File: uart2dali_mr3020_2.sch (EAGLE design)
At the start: 79 parts, among them IC2 LM393D, IC3 SFH6156, IC4 SFH6156, J1 AVR_SPI_PRG_6NS, Q1 SST201, Q2 BSP170P, Q3 BC817-25SMD, X1 SM04B-SRSS-TB

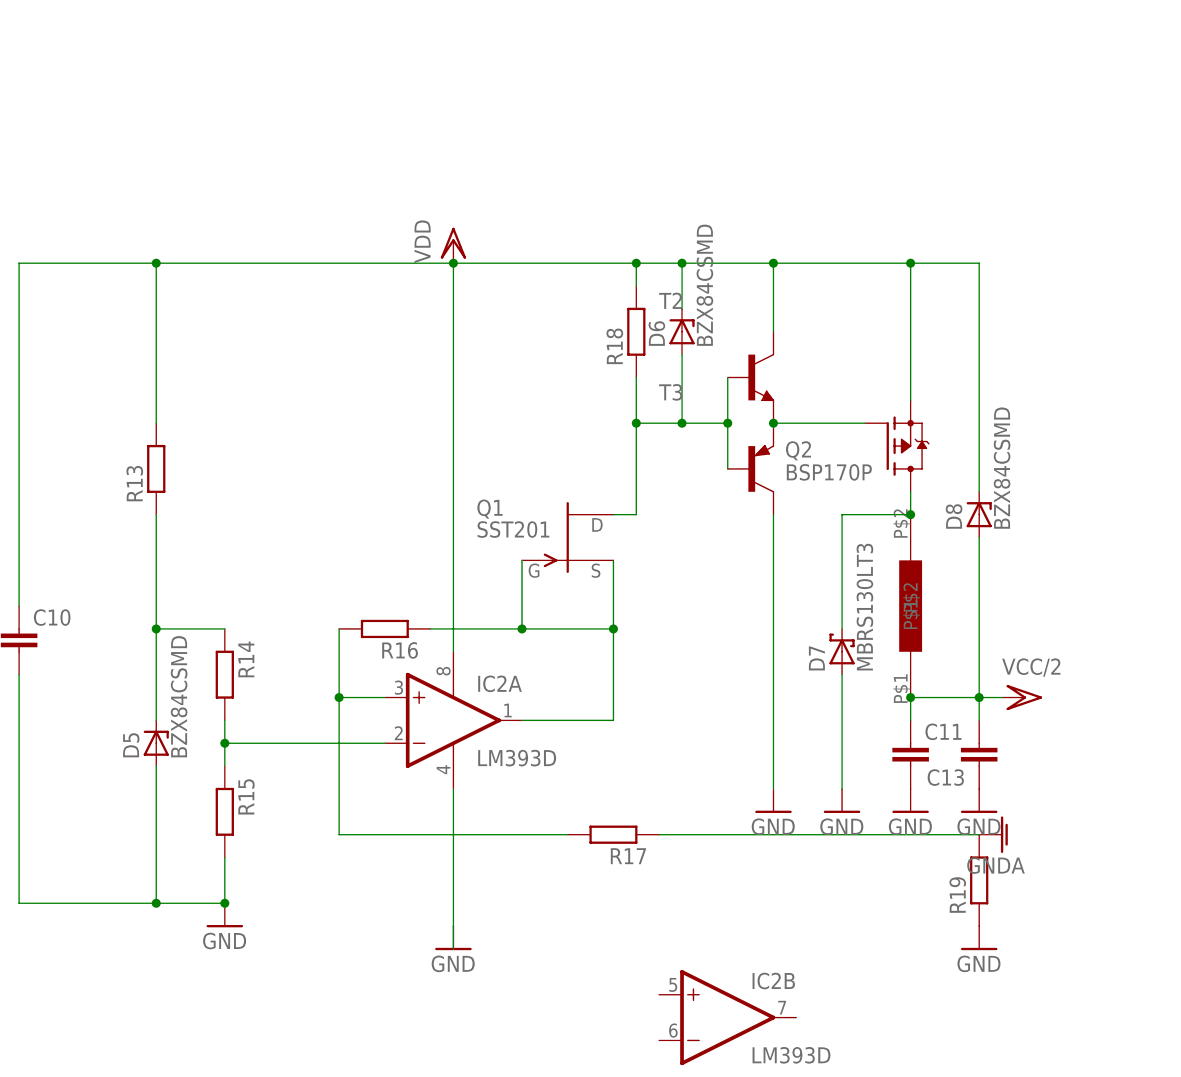
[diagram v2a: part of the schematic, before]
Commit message: - added values parts of constant current circuit - dali master can query from slaves
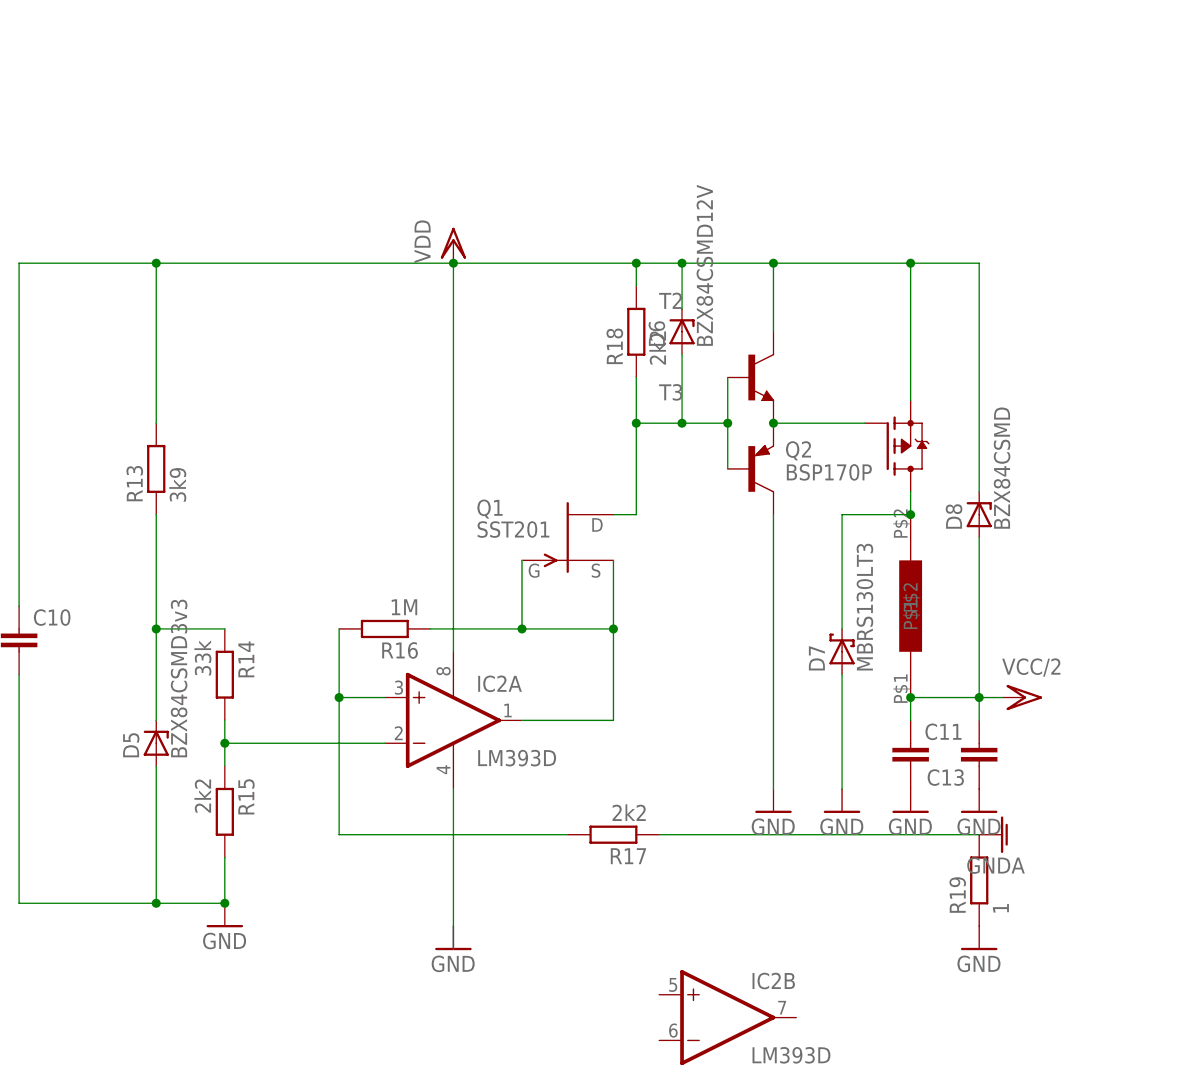
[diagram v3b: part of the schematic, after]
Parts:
- D5: value BZX84CSMD -> BZX84CSMD3v3
- D6: value BZX84CSMD -> BZX84CSMD12V
- R13: value (none) -> 3k9
- R14: value (none) -> 33k
- R15, R17, R18: value (none) -> 2k2
- R16: value (none) -> 1M
- R19: value (none) -> 1
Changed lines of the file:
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@@
 <part name="P+13" library="supply1" deviceset="VCC/2" device=""/>
 <part name="GND24" library="supply1" deviceset="GNDA" device=""/>
-<part name="R19" library="resistor" deviceset="R-EU_" device="R0603"/>
+<part name="R19" library="resistor" deviceset="R-EU_" device="R0603" value="1"/>
 <part name="D7" library="diode" deviceset="MBRS130LT3" device=""/>
 <part name="GND25" library="supply1" deviceset="GND" device=""/>
 <part name="GND26" library="supply1" deviceset="GND" device=""/>
-<part name="R18" library="resistor" deviceset="R-EU_" device="R0603"/>
-<part name="R13" library="resistor" deviceset="R-EU_" device="R0603"/>
+<part name="R18" library="resistor" deviceset="R-EU_" device="R0603" value="2k2"/>
+<part name="R13" library="resistor" deviceset="R-EU_" device="R0603" value="3k9"/>
 <part name="C11" library="resistor" deviceset="C-EU" device="C0805"/>
 <part name="GND28" library="supply1" deviceset="GND" device=""/>
 <part name="GND29" library="supply1" deviceset="GND" device=""/>
-<part name="R17" library="resistor" deviceset="R-EU_" device="R0603"/>
-<part name="R16" library="resistor" deviceset="R-EU_" device="R0603"/>
+<part name="R17" library="resistor" deviceset="R-EU_" device="R0603" value="2k2"/>
+<part name="R16" library="resistor" deviceset="R-EU_" device="R0603" value="1M"/>
 <part name="GND30" library="supply1" deviceset="GND" device=""/>
-<part name="D6" library="diode" deviceset="BZX84CSMD" device=""/>
-<part name="R15" library="resistor" deviceset="R-EU_" device="R0603"/>
-<part name="R14" library="resistor" deviceset="R-EU_" device="R0603"/>
-<part name="D5" library="diode" deviceset="BZX84CSMD" device=""/>
+<part name="D6" library="diode" deviceset="BZX84CSMD" device="" value="BZX84CSMD12V"/>
+<part name="R15" library="resistor" deviceset="R-EU_" device="R0603" value="2k2"/>
+<part name="R14" library="resistor" deviceset="R-EU_" device="R0603" value="33k"/>
+<part name="D5" library="diode" deviceset="BZX84CSMD" device="" value="BZX84CSMD3v3"/>
 <part name="C10" library="resistor" deviceset="C-EU" device="C0603"/>
 <part name="GND31" library="supply1" deviceset="GND" device=""/>

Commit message: got dali master firmware to a "working" state
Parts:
- added J2: (no value), con-jack:JACK-PLUG1
- added R27: 10k, resistor:R-EU_R0603
- added T4: (no value), transistor:MMBT3904LT1-NPN-SOT23-BEC
- added X2: 22-23-2021, con-molex:22-23-2021
- R10, R26, R7, R9: value (none) -> 10k
- R20: value (none) -> 1k2
- R21: value (none) -> 330
- R22: value (none) -> 3k
- R23: value (none) -> 0
- R25: value (none) -> 11k
- R5: value (none) -> 3k3
- R6, R8: value (none) -> 2k2
- T1: device transistor:-NPN-SOT23-EBC -> transistor:MMBT3904LT1-NPN-SOT23-BEC
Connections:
- net +5V: now also R27.1
- net D+: now also B1.-; no longer B1.+
- net D-: now also B1.+; no longer B1.-
- net DALI_RCV: now also R27.2, T4.B, T4.C
- net GND: now also T4.E
- net VDD: no longer D8.C
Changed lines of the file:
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@@
 <part name="D11" library="diode" deviceset="BZX84CSMD" device="" value="BZX84CSMD 2V7"/>
 <part name="D9" library="diode" deviceset="BZX85" device=""/>
-<part name="R25" library="resistor" deviceset="R-EU_" device="R0603"/>
-<part name="R23" library="resistor" deviceset="R-EU_" device="R0603"/>
+<part name="R25" library="resistor" deviceset="R-EU_" device="R0603" value="11k"/>
+<part name="R23" library="resistor" deviceset="R-EU_" device="R0603" value="0"/>
 <part name="R24" library="resistor" deviceset="R-EU_" device="R0603" value="4R7"/>
-<part name="R21" library="resistor" deviceset="R-EU_" device="R0603"/>
-<part name="R22" library="resistor" deviceset="R-EU_" device="R0603"/>
+<part name="R21" library="resistor" deviceset="R-EU_" device="R0603" value="330"/>
+<part name="R22" library="resistor" deviceset="R-EU_" device="R0603" value="3k"/>
 <part name="C12" library="resistor" deviceset="CPOL-EU" device="CT6032"/>
-<part name="R20" library="resistor" deviceset="R-EU_" device="R0603"/>
+<part name="R20" library="resistor" deviceset="R-EU_" device="R0603" value="1k2"/>
 <part name="GND2" library="supply1" deviceset="GND" device=""/>
-<part name="R26" library="resistor" deviceset="R-EU_" device="R0603"/>
+<part name="R26" library="resistor" deviceset="R-EU_" device="R0603" value="10k"/>
 <part name="P+1" library="supply1" deviceset="+5V" device=""/>
 <part name="P+2" library="supply1" deviceset="+5V" device=""/>
@@
 <part name="GND6" library="supply1" deviceset="GND" device=""/>
 <part name="P+7" library="supply1" deviceset="+5V" device=""/>
-<part name="R7" library="resistor" deviceset="R-EU_" device="R0603"/>
+<part name="R7" library="resistor" deviceset="R-EU_" device="R0603" value="10k"/>
 <part name="C9" library="resistor" deviceset="C-EU" device="C0603"/>
 <part name="P+10" library="supply1" deviceset="+5V" device=""/>
@@
 <part name="Y1" library="SparkFun-FreqCtrl" deviceset="CRYSTAL" device="TXC-7A"/>
 <part name="J1" library="SparkFun-Connectors" deviceset="AVR_SPI_PRG_6" device="NS"/>
-<part name="R6" library="resistor" deviceset="R-EU_" device="R0603"/>
-<part name="R5" library="resistor" deviceset="R-EU_" device="R0603"/>
+<part name="R6" library="resistor" deviceset="R-EU_" device="R0603" value="2k2"/>
+<part name="R5" library="resistor" deviceset="R-EU_" device="R0603" value="3k3"/>
 <part name="GND8" library="supply1" deviceset="GND" device=""/>
-<part name="R9" library="resistor" deviceset="R-EU_" device="R0603"/>
-<part name="R10" library="resistor" deviceset="R-EU_" device="R0603"/>
-<part name="R8" library="resistor" deviceset="R-EU_" device="R0603"/>
-<part name="T1" library="transistor" deviceset="*-NPN-" device="SOT23-EBC"/>
+<part name="R9" library="resistor" deviceset="R-EU_" device="R0603" value="10k"/>
+<part name="R10" library="resistor" deviceset="R-EU_" device="R0603" value="10k"/>
+<part name="R8" library="resistor" deviceset="R-EU_" device="R0603" value="2k2"/>
+<part name="T1" library="transistor" deviceset="*-NPN-" device="SOT23-BEC" technology="MMBT3904LT1"/>
 <part name="GND20" library="supply1" deviceset="GND" device=""/>
 <part name="P+11" library="supply1" deviceset="+5V" device=""/>
@@
 <part name="VDD5" library="supply1" deviceset="VDD" device=""/>
 <part name="VDD6" library="supply1" deviceset="VDD" device=""/>
+<part name="T4" library="transistor" deviceset="*-NPN-" device="SOT23-BEC" technology="MMBT3904LT1"/>
+<part name="R27" library="resistor" deviceset="R-EU_" device="R0603" value="10k"/>
+<part name="P+3" library="supply1" deviceset="+5V" device=""/>
+<part name="GND33" library="supply1" deviceset="GND" device=""/>
+<part name="X2" library="con-molex" deviceset="22-23-2021" device=""/>
+<part name="J2" library="con-jack" deviceset="JACK-PLUG" device="1"/>
 </parts>
 <sheets>
@@
 <instance part="IC4" gate="CE" x="563.88" y="66.04"/>
 <instance part="IC4" gate="LED" x="553.72" y="66.04"/>
-<instance part="B1" gate="G$1" x="541.02" y="96.52"/>
+<instance part="B1" gate="G$1" x="541.02" y="96.52" rot="MR0"/>
 <instance part="Q3" gate="G$1" x="530.86" y="43.18"/>
 <instance part="D10" gate="1" x="525.78" y="71.12" rot="R180"/>
@@
 <instance part="VDD5" gate="G$1" x="17.78" y="116.84"/>
 <instance part="VDD6" gate="G$1" x="25.4" y="116.84"/>
+<instance part="T4" gate="G$1" x="574.04" y="73.66"/>
+<instance part="R27" gate="G$1" x="576.58" y="83.82" rot="R270"/>
+<instance part="P+3" gate="1" x="576.58" y="91.44"/>
+<instance part="GND33" gate="1" x="576.58" y="50.8"/>
+<instance part="X2" gate="-1" x="127" y="139.7"/>
+<instance part="X2" gate="-2" x="127" y="137.16"/>
+<instance part="J2" gate="G$1" x="119.38" y="116.84"/>
 </instances>
 <busses>
@@
 <junction x="525.78" y="27.94"/>
 <junction x="533.4" y="27.94"/>
-<pinref part="B1" gate="G$1" pin="+"/>
-<wire x1="546.1" y1="96.52" x2="581.66" y2="96.52" width="0.1524" layer="91"/>
-<wire x1="581.66" y1="96.52" x2="581.66" y2="27.94" width="0.1524" layer="91"/>
-<wire x1="581.66" y1="27.94" x2="558.8" y2="27.94" width="0.1524" layer="91"/>
+<wire x1="596.9" y1="96.52" x2="596.9" y2="27.94" width="0.1524" layer="91"/>
+<wire x1="596.9" y1="27.94" x2="558.8" y2="27.94" width="0.1524" layer="91"/>
 <junction x="546.1" y="27.94"/>
 <pinref part="TP18" gate="G$1" pin="TP"/>
@@
 <junction x="558.8" y="27.94"/>
 <label x="556.26" y="96.52" size="1.778" layer="95"/>
+<pinref part="B1" gate="G$1" pin="-"/>
+<wire x1="546.1" y1="96.52" x2="596.9" y2="96.52" width="0.1524" layer="91"/>
 </segment>
 </net>
@@
 <pinref part="R23" gate="G$1" pin="1"/>
 <wire x1="533.4" y1="86.36" x2="533.4" y2="96.52" width="0.1524" layer="91"/>
-<pinref part="B1" gate="G$1" pin="-"/>
+<label x="533.4" y="93.98" size="1.778" layer="95" rot="R90"/>
+<pinref part="B1" gate="G$1" pin="+"/>
 <wire x1="533.4" y1="96.52" x2="535.94" y2="96.52" width="0.1524" layer="91"/>
-<label x="533.4" y="93.98" size="1.778" layer="95" rot="R90"/>
 </segment>
 </net>
@@
 <pinref part="C15" gate="G$1" pin="2"/>
 <pinref part="GND32" gate="1" pin="GND"/>
+</segment>
+<segment>
+<pinref part="T4" gate="G$1" pin="E"/>
+<pinref part="GND33" gate="1" pin="GND"/>
+<wire x1="576.58" y1="53.34" x2="576.58" y2="68.58" width="0.1524" layer="91"/>
 </segment>
 </net>
@@
 <junction x="254" y="129.54"/>
 </segment>
+<segment>
+<pinref part="R27" gate="G$1" pin="1"/>
+<pinref part="P+3" gate="1" pin="+5V"/>
+</segment>
 </net>
 <net name="DALI_RCV" class="0">
@@
 <pinref part="R26" gate="G$1" pin="2"/>
 <pinref part="IC4" gate="CE" pin="C"/>
-<wire x1="566.42" y1="76.2" x2="566.42" y2="71.12" width="0.1524" layer="91"/>
-<wire x1="566.42" y1="76.2" x2="576.58" y2="76.2" width="0.1524" layer="91"/>
-<junction x="566.42" y="76.2"/>
-<label x="568.96" y="76.2" size="1.778" layer="95"/>
+<wire x1="566.42" y1="76.2" x2="566.42" y2="73.66" width="0.1524" layer="91"/>
+<pinref part="T4" gate="G$1" pin="B"/>
+<wire x1="566.42" y1="73.66" x2="566.42" y2="71.12" width="0.1524" layer="91"/>
+<wire x1="571.5" y1="73.66" x2="566.42" y2="73.66" width="0.1524" layer="91"/>
+<junction x="566.42" y="73.66"/>
 </segment>
 <segment>
@@
 <label x="271.78" y="40.64" size="1.778" layer="95"/>
 <pinref part="J1" gate="G$1" pin="3"/>
+</segment>
+<segment>
+<pinref part="T4" gate="G$1" pin="C"/>
+<pinref part="R27" gate="G$1" pin="2"/>
+<wire x1="576.58" y1="78.74" x2="586.74" y2="78.74" width="0.1524" layer="91"/>
+<junction x="576.58" y="78.74"/>
+<label x="579.12" y="78.74" size="1.778" layer="95"/>
 </segment>
 </net>
@@
 <wire x1="337.82" y1="106.68" x2="353.06" y2="106.68" width="0.1524" layer="91"/>
 <junction x="353.06" y="106.68"/>
-<pinref part="D8" gate="G$1" pin="C"/>
-<wire x1="444.5" y1="81.28" x2="444.5" y2="106.68" width="0.1524" layer="91"/>
 <wire x1="444.5" y1="106.68" x2="436.88" y2="106.68" width="0.1524" layer="91"/>
 <junction x="421.64" y="106.68"/>
